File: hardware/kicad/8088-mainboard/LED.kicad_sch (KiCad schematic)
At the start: 20 parts, among them U10 74LS273, U11 74LS00

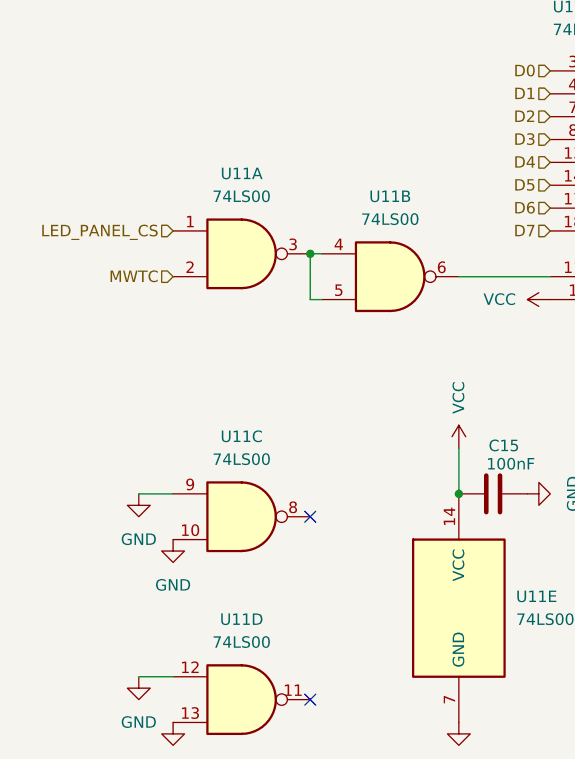
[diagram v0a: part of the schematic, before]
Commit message: Update 8088-mainboard schematics for refined connections and label adjustments
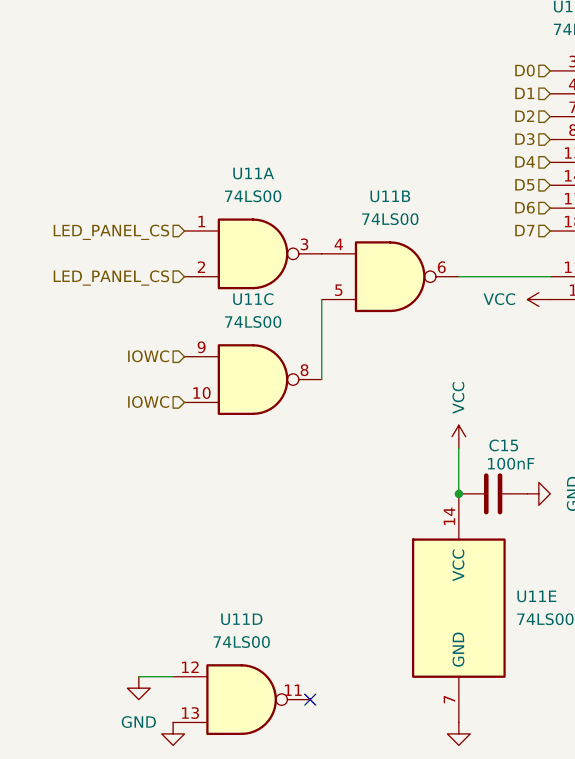
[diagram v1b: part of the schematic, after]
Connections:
- net MWTC is gone; now on net LED_PANEL_CS: U11.2
- net GND: no longer U11.10, U11.9
- net at U11.3, U11.4: no longer U11.5
- net at U11.8: now also U11.5
- new net IOWC: U11.10, U11.9
- no-connect marks 2 -> 1
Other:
- moved on the sheet: U11A, U11C
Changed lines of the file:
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@@
-	)
-	(junction
-		(at 68.58 95.25)
-		(diameter 0)
-		(color 0 0 0 0)
 	)
 	(junction
@@
 	)
 	(no_connect
-		(at 68.58 124.46)
-	)
-	(no_connect
 		(at 68.58 144.78)
 	)
@@
 	(wire
 		(pts
-			(xy 85.09 97.79) (xy 95.25 97.79)
+			(xy 69.85 100.33) (xy 69.85 109.22)
 		)
 		(stroke
@@
 	(wire
 		(pts
-			(xy 120.65 77.47) (xy 134.62 77.47)
+			(xy 85.09 97.79) (xy 95.25 97.79)
 		)
 		(stroke
@@
 	(wire
 		(pts
-			(xy 68.58 100.33) (xy 68.58 95.25)
+			(xy 120.65 77.47) (xy 134.62 77.47)
 		)
 		(stroke
@@
 	(wire
 		(pts
-			(xy 49.53 121.92) (xy 53.34 121.92)
+			(xy 49.53 142.24) (xy 53.34 142.24)
 		)
 		(stroke
@@
 	(wire
 		(pts
-			(xy 49.53 142.24) (xy 53.34 142.24)
+			(xy 107.95 67.31) (xy 107.95 62.23)
 		)
 		(stroke
@@
 	(wire
 		(pts
-			(xy 107.95 67.31) (xy 107.95 62.23)
-		)
-		(stroke
-			(width 0)
-			(type default)
-		)
-	)
-	(wire
-		(pts
 			(xy 120.65 80.01) (xy 143.51 80.01)
-		)
-		(stroke
-			(width 0)
-			(type default)
-		)
-	)
-	(wire
-		(pts
-			(xy 69.85 95.25) (xy 68.58 95.25)
-		)
-		(stroke
-			(width 0)
-			(type default)
-		)
-	)
-	(wire
-		(pts
-			(xy 69.85 100.33) (xy 68.58 100.33)
 		)
 		(stroke
@@
 		)
 	)
+	(hierarchical_label "LED_PANEL_CS"
+		(shape input)
+		(at 54.61 97.79 180)
+		(effects
+			(font
+				(size 1.27 1.27)
+			)
+			(justify right)
+		)
+	)
 	(hierarchical_label "D2"
 		(shape input)
@@
 		)
 	)
-	(hierarchical_label "MWTC"
+	(hierarchical_label "IOWC"
 		(shape input)
-		(at 53.34 97.79 180)
+		(at 54.61 106.68 180)
 		(effects
 			(font
@@
 		)
 	)
+	(hierarchical_label "IOWC"
+		(shape input)
+		(at 54.61 111.76 180)
+		(effects
+			(font
+				(size 1.27 1.27)
+			)
+			(justify right)
+		)
+	)
 	(hierarchical_label "D0"
 		(shape input)
@@
 	(hierarchical_label "LED_PANEL_CS"
 		(shape input)
-		(at 53.34 92.71 180)
+		(at 54.61 92.71 180)
 		(effects
 			(font
@@
 	(symbol
 		(lib_id "74xx:74LS00")
-		(at 60.96 95.25 0)
+		(at 62.23 95.25 0)
 		(unit 1)
 		(body_style 1)
@@
 		(fields_autoplaced yes)
 		(property "Reference" "U11"
-			(at 60.9517 86.36 0)
+			(at 62.2217 86.36 0)
 			(show_name no)
 			(do_not_autoplace no)
@@
 		)
 		(property "Value" "74LS00"
-			(at 60.9517 88.9 0)
+			(at 62.2217 88.9 0)
 			(show_name no)
 			(do_not_autoplace no)
@@
 		)
 		(property "Footprint" "Package_DIP:DIP-14_W7.62mm"
-			(at 60.96 95.25 0)
+			(at 62.23 95.25 0)
 			(hide yes)
 			(show_name no)
@@
 		)
 		(property "Datasheet" "http://www.ti.com/lit/gpn/sn74ls00"
-			(at 60.96 95.25 0)
+			(at 62.23 95.25 0)
 			(hide yes)
 			(show_name no)
@@
 		)
 		(property "Description" "quad 2-input NAND gate"
-			(at 60.96 95.25 0)
+			(at 62.23 95.25 0)
 			(hide yes)
 			(show_name no)
@@
 	)
 	(symbol
-		(lib_id "power:GND")
-		(at 53.34 127 0)
-		(unit 1)
-		(body_style 1)
-		(exclude_from_sim no)
-		(in_bom yes)
-		(on_board yes)
-		(in_pos_files yes)
-		(dnp no)
-		(fields_autoplaced yes)
-		(property "Reference" "#PWR068"
-			(at 53.34 133.35 0)
-			(hide yes)
-			(show_name no)
-			(do_not_autoplace no)
-			(effects
-				(font
-					(size 1.27 1.27)
-				)
-			)
-		)
-		(property "Value" "GND"
-			(at 53.34 132.08 0)
-			(show_name no)
-			(do_not_autoplace no)
-			(effects
-				(font
-					(size 1.27 1.27)
-				)
-			)
-		)
-		(property "Footprint" ""
-			(at 53.34 127 0)
-			(hide yes)
-			(show_name no)
-			(do_not_autoplace no)
-			(effects
-				(font
-					(size 1.27 1.27)
-				)
-			)
-		)
-		(property "Datasheet" ""
-			(at 53.34 127 0)
-			(hide yes)
-			(show_name no)
-			(do_not_autoplace no)
-			(effects
-				(font
-					(size 1.27 1.27)
-				)
-			)
-		)
-		(property "Description" "Power symbol creates a global label with name \"GND\" , ground"
-			(at 53.34 127 0)
-			(hide yes)
-			(show_name no)
-			(do_not_autoplace no)
-			(effects
-				(font
-					(size 1.27 1.27)
-				)
-			)
-		)
-		(pin "1"
-		)
-		(instances
-			(project "8088-mainboard"
-				(path "/15ce4f45-6f32-456e-874c-aac11293789a/84282b2b-43ee-46fa-876b-fa0b647a45d9"
-					(reference "#PWR068")
-					(unit 1)
-				)
-			)
-		)
-	)
-	(symbol
 		(lib_id "Device:R")
 		(at 161.29 73.66 0)
@@
 	)
 	(symbol
-		(lib_id "power:GND")
-		(at 49.53 121.92 0)
-		(unit 1)
-		(body_style 1)
-		(exclude_from_sim no)
-		(in_bom yes)
-		(on_board yes)
-		(in_pos_files yes)
-		(dnp no)
-		(fields_autoplaced yes)
-		(property "Reference" "#PWR067"
-			(at 49.53 128.27 0)
-			(hide yes)
-			(show_name no)
-			(do_not_autoplace no)
-			(effects
-				(font
-					(size 1.27 1.27)
-				)
-			)
-		)
-		(property "Value" "GND"
-			(at 49.53 127 0)
-			(show_name no)
-			(do_not_autoplace no)
-			(effects
-				(font
-					(size 1.27 1.27)
-				)
-			)
-		)
-		(property "Footprint" ""
-			(at 49.53 121.92 0)
-			(hide yes)
-			(show_name no)
-			(do_not_autoplace no)
-			(effects
-				(font
-					(size 1.27 1.27)
-				)
-			)
-		)
-		(property "Datasheet" ""
-			(at 49.53 121.92 0)
-			(hide yes)
-			(show_name no)
-			(do_not_autoplace no)
-			(effects
-				(font
-					(size 1.27 1.27)
-				)
-			)
-		)
-		(property "Description" "Power symbol creates a global label with name \"GND\" , ground"
-			(at 49.53 121.92 0)
-			(hide yes)
-			(show_name no)
-			(do_not_autoplace no)
-			(effects
-				(font
-					(size 1.27 1.27)
-				)
-			)
-		)
-		(pin "1"
-		)
-		(instances
-			(project "8088-mainboard"
-				(path "/15ce4f45-6f32-456e-874c-aac11293789a/84282b2b-43ee-46fa-876b-fa0b647a45d9"
-					(reference "#PWR067")
-					(unit 1)
-				)
-			)
-		)
-	)
-	(symbol
 		(lib_id "Device:LED")
 		(at 134.62 73.66 90)
@@
 	(symbol
 		(lib_id "74xx:74LS00")
-		(at 60.96 124.46 0)
+		(at 62.23 109.22 0)
 		(unit 3)
 		(body_style 1)
@@
 		(fields_autoplaced yes)
 		(property "Reference" "U11"
-			(at 60.9517 115.57 0)
+			(at 62.2217 100.33 0)
 			(show_name no)
 			(do_not_autoplace no)
@@
 		)
 		(property "Value" "74LS00"
-			(at 60.9517 118.11 0)
+			(at 62.2217 102.87 0)
 			(show_name no)
 			(do_not_autoplace no)
@@
 		)
 		(property "Footprint" "Package_DIP:DIP-14_W7.62mm"
-			(at 60.96 124.46 0)
+			(at 62.23 109.22 0)
 			(hide yes)
 			(show_name no)
@@
 		)
 		(property "Datasheet" "http://www.ti.com/lit/gpn/sn74ls00"
-			(at 60.96 124.46 0)
+			(at 62.23 109.22 0)
 			(hide yes)
 			(show_name no)
@@
 		)
 		(property "Description" "quad 2-input NAND gate"
-			(at 60.96 124.46 0)
-			(hide yes)
-			(show_name no)
+			(at 62.23 109.22 0)
+			(hide yes)
+			(show_name no)

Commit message: Update 8086-mainboard scheme
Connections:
- net GND: now also U11.10, U11.9; no longer U11.12, U11.13
- net IOWC: now also U11.1, U11.2; no longer U11.10, U11.9
- net LED_PANEL_CS: now also U11.4, U11.5; no longer U11.1, U11.2
- net at U11.3: now also U11.12; no longer U11.4
- net at U11.11: now also U10.11 (Cp)
- net at U11.8: no longer U11.5
- net at U11.6: now also U11.13; no longer U10.11 (Cp)
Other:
- moved on the sheet: U11A, U11B, U11C, U11D

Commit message: Update 8088-mainboard schematics
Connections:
- net IOWC renamed IOM
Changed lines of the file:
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@@
 		)
 	)
-	(hierarchical_label "IOWC"
+	(hierarchical_label "IOM"
 		(shape input)
 		(at 46.99 97.79 180)
@@
 		)
 	)
-	(hierarchical_label "IOWC"
+	(hierarchical_label "IOM"
 		(shape input)
 		(at 46.99 92.71 180)
